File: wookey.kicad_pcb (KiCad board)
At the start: 4 copper layers, 43 x 66 mm, 90 parts, among them P1 GND, P1000 ISO7816_NO, P1900 CONN_FPC16, P3000 USB_FS_OTG, P513 TP1, P514 TP2, P515 TP3, P523 UART4, P542 TP4, P543 TP5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

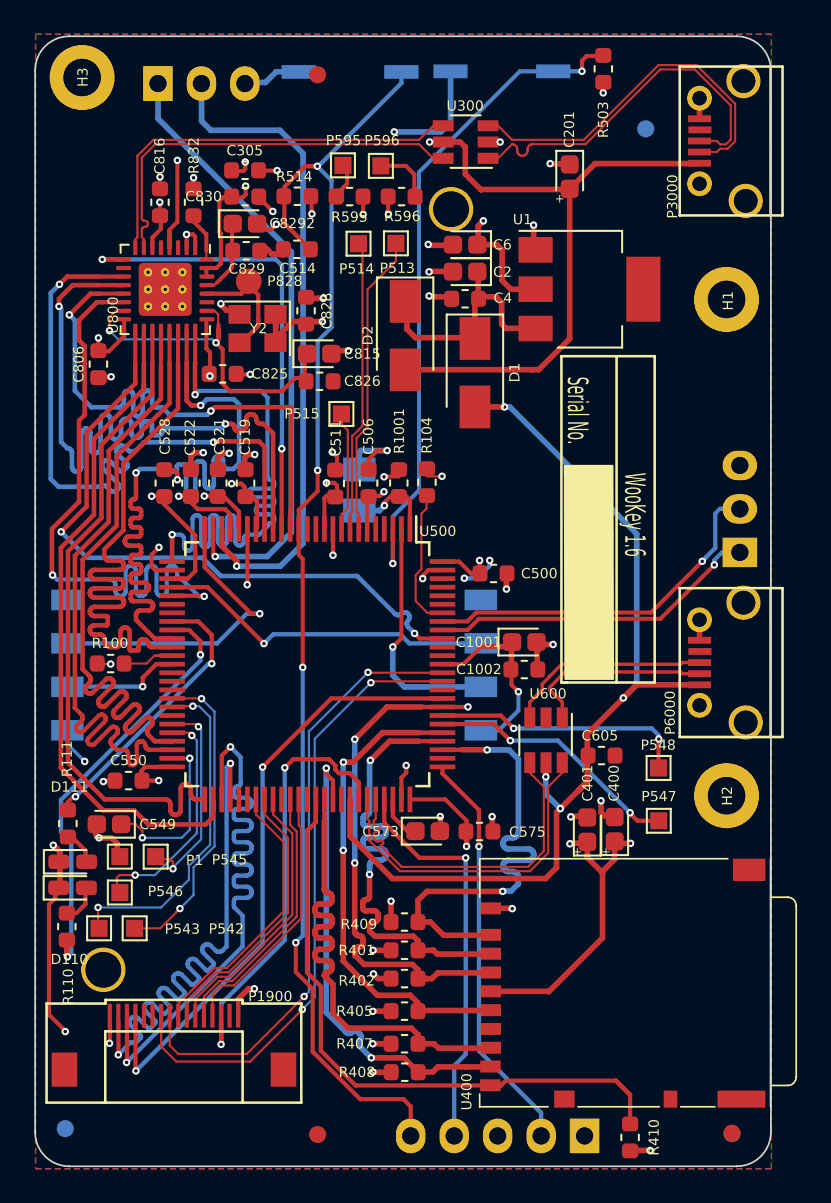
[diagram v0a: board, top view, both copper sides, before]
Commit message: [enhancement] add pcb screenshots
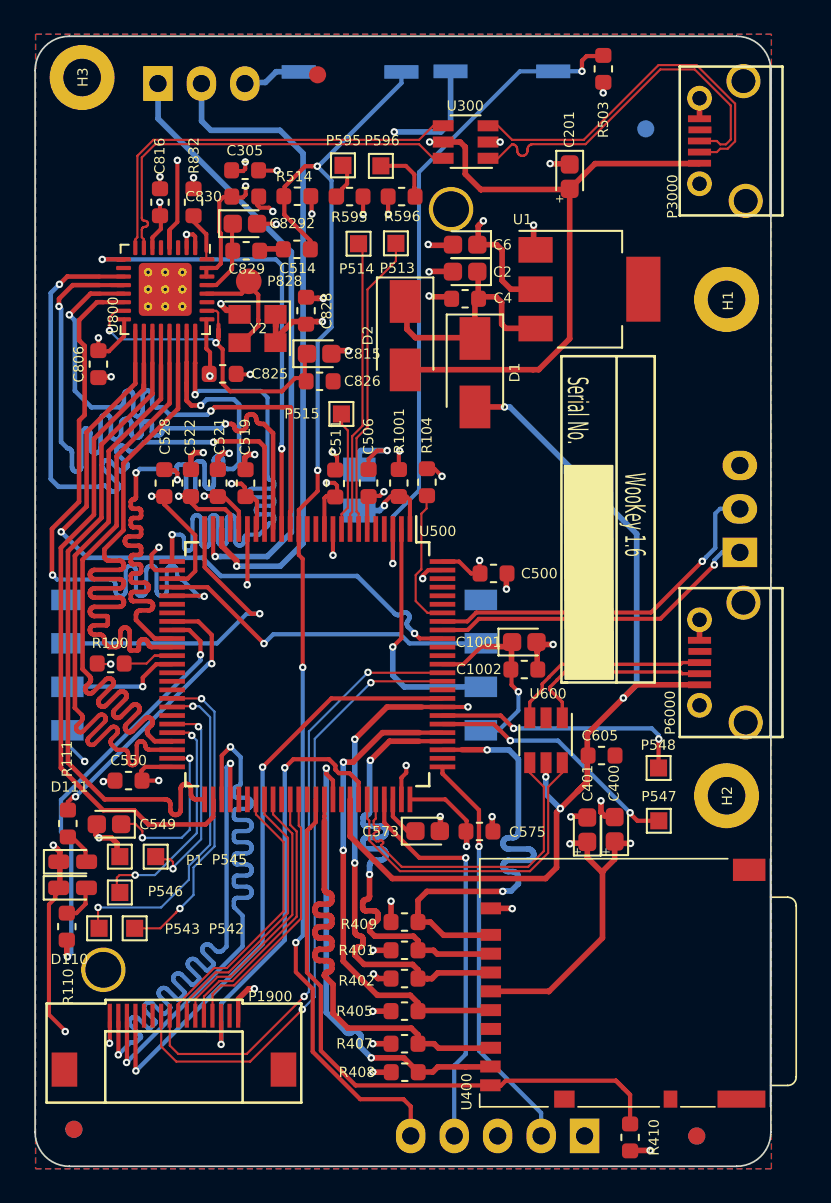
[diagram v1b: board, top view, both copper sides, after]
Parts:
- moved FID3 14.2 mm to (88.2, 103.7)
- moved FID1 2.07 mm to (124.6, 104.1)
- moved FID6 2.07 mm to (124.6, 104.1)
- moved FID4 0.51 mm to (88.2, 103.7)
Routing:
- net /rfid/INT0: track 2.14 -> 0.00 mm, vias 2 -> 0
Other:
- board text added: "The current 4 layer 1.6mm board stackup is as follows: Thickness Layer ======================================== 0.0356mm copper 0.1702mm FR408 prepreg 0.0178mm copper 1.1938mm FR408 0.0178mm copper 0.1702mm FR408 prepreg 0.0356mm copper 0.0254mm solder resist"
- board text removed: "The current 4 layer 0.8mm board stackup is as follows: Thickness Layer ================================================ 35µm copper 175µm 7628LR-TG150 35µm copper 250µm 35µm copper 175µm 7628LR-TG150 35µm copper"
